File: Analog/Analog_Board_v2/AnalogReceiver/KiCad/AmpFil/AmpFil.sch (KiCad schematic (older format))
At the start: 47 parts, among them P1 CONN_01X02, P10 CONN_01X02, P11 CONN_01X02, P2 CONN_01X02, P3 CONN_01X02, P4 CONN_01X02, P5 CONN_01X02, P6 CONN_01X02, P7 CONN_01X02, P8 CONN_01X02, P9 CONN_01X02, U1 LT1677, U2 SiPM, U3 LT1677, U4 LT1677, U5 LT1677

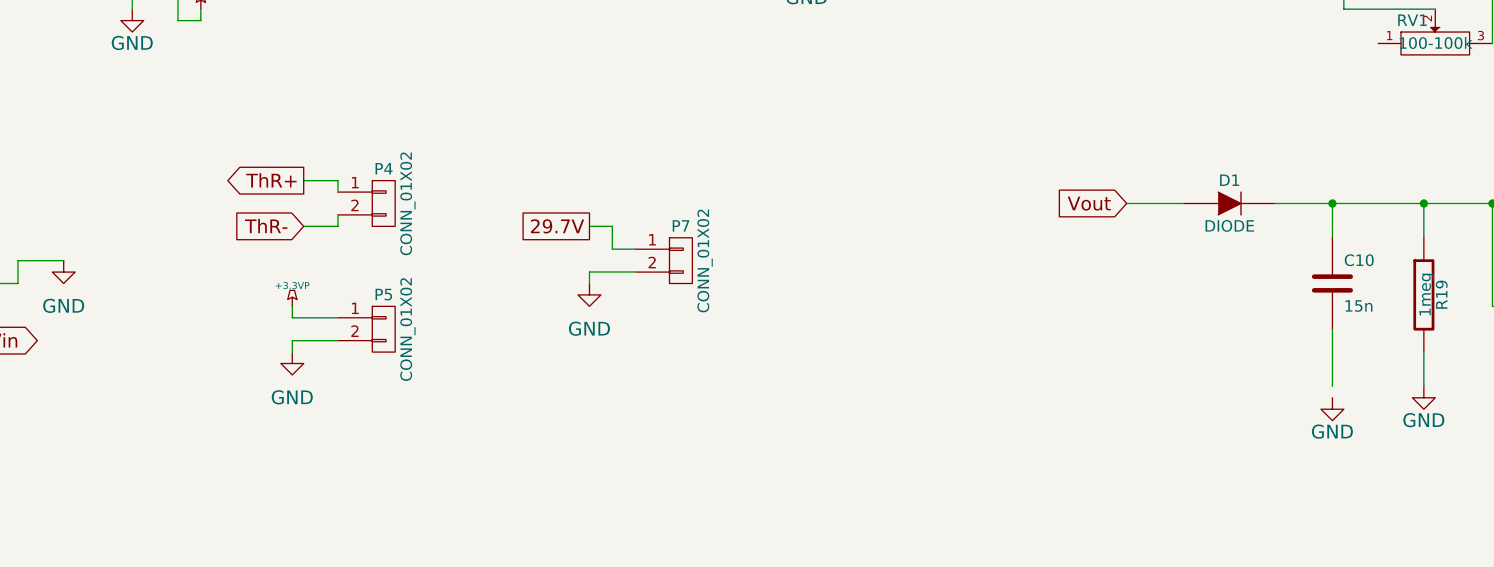
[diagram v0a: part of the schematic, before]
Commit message: New Cutoffs
I tweaked the designs to give different cutoff frequencies and ripple
levels.
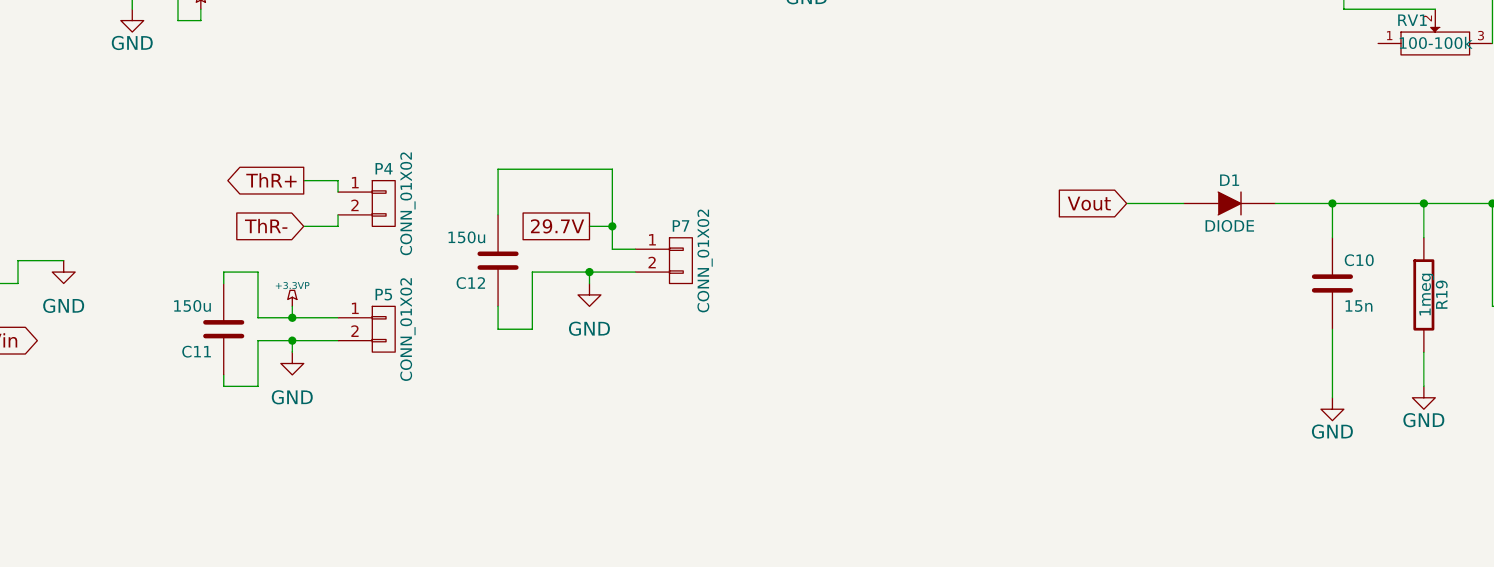
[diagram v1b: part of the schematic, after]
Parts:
- added C11, C12: 150u, symbol C
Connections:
- net +3.3VP: now also C11.2
- net 29.7V: now also C12.2
- net GND: now also C10.2, C11.1, C12.1
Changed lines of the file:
@@
 $EndComp
 $Comp
-L GND #PWR2
+L GND #PWR01
 U 1 1 54DB8B2B
 P 1300 2450
-F 0 "#PWR2" H 1300 2200 60  0001 C CNN
+F 0 "#PWR01" H 1300 2200 60  0001 C CNN
 F 1 "GND" H 1300 2300 60  0000 C CNN
 F 2 "" H 1300 2450 60  0000 C CNN
@@
 $EndComp
 $Comp
-L GND #PWR3
+L GND #PWR02
 U 1 1 54DB8B4B
 P 1600 1450
-F 0 "#PWR3" H 1600 1200 60  0001 C CNN
+F 0 "#PWR02" H 1600 1200 60  0001 C CNN
 F 1 "GND" H 1600 1250 60  0000 C CNN
 F 2 "" H 1600 1450 60  0000 C CNN
@@
 $EndComp
 $Comp
-L GND #PWR5
+L GND #PWR03
 U 1 1 54DB8B6B
 P 2250 1750
-F 0 "#PWR5" H 2250 1500 60  0001 C CNN
+F 0 "#PWR03" H 2250 1500 60  0001 C CNN
 F 1 "GND" H 2250 1600 60  0000 C CNN
 F 2 "" H 2250 1750 60  0000 C CNN
@@
 $EndComp
 $Comp
-L +3.3VP #PWR4
+L +3.3VP #PWR04
 U 1 1 54DB8B8B
 P 1850 1450
-F 0 "#PWR4" H 1900 1480 20  0001 C CNN
+F 0 "#PWR04" H 1900 1480 20  0001 C CNN
 F 1 "+3.3VP" H 1850 1540 30  0000 C CNN
 F 2 "" H 1850 1450 60  0000 C CNN
@@
 $EndComp
 $Comp
-L +3.3VP #PWR6
+L +3.3VP #PWR05
 U 1 1 54DB8BBE
 P 2250 2350
-F 0 "#PWR6" H 2300 2380 20  0001 C CNN
+F 0 "#PWR05" H 2300 2380 20  0001 C CNN
 F 1 "+3.3VP" H 2250 2440 30  0000 C CNN
 F 2 "" H 2250 2350 60  0000 C CNN
@@
 $EndComp
 $Comp
-L +3.3VP #PWR1
+L +3.3VP #PWR06
 U 1 1 54DB8BDE
 P 1100 2350
-F 0 "#PWR1" H 1150 2380 20  0001 C CNN
+F 0 "#PWR06" H 1150 2380 20  0001 C CNN
 F 1 "+3.3VP" H 1100 2440 30  0000 C CNN
 F 2 "" H 1100 2350 60  0000 C CNN
@@
 $EndComp
 $Comp
-L GND #PWR10
+L GND #PWR07
 U 1 1 54DBE1F2
 P 3950 2750
-F 0 "#PWR10" H 3950 2500 60  0001 C CNN
+F 0 "#PWR07" H 3950 2500 60  0001 C CNN
 F 1 "GND" H 3950 2600 60  0000 C CNN
 F 2 "" H 3950 2750 60  0000 C CNN
@@
 $EndComp
 $Comp
-L GND #PWR12
+L GND #PWR08
 U 1 1 54DBE232
 P 4550 1900
-F 0 "#PWR12" H 4550 1650 60  0001 C CNN
+F 0 "#PWR08" H 4550 1650 60  0001 C CNN
 F 1 "GND" H 4550 1750 60  0000 C CNN
 F 2 "" H 4550 1900 60  0000 C CNN
@@
 $EndComp
 $Comp
-L +3.3VP #PWR11
+L +3.3VP #PWR09
 U 1 1 54DBE272
 P 4250 2750
-F 0 "#PWR11" H 4300 2780 20  0001 C CNN
+F 0 "#PWR09" H 4300 2780 20  0001 C CNN
 F 1 "+3.3VP" H 4250 2840 30  0000 C CNN
 F 2 "" H 4250 2750 60  0000 C CNN
@@
 $EndComp
 $Comp
-L +3.3VP #PWR15
+L +3.3VP #PWR010
 U 1 1 54DBE2B2
 P 4700 2350
-F 0 "#PWR15" H 4750 2380 20  0001 C CNN
+F 0 "#PWR010" H 4750 2380 20  0001 C CNN
 F 1 "+3.3VP" H 4700 2440 30  0000 C CNN
 F 2 "" H 4700 2350 60  0000 C CNN
@@
 Connection ~ 7700 2100
 $Comp
-L GND #PWR16
+L GND #PWR011
 U 1 1 54DC07DF
 P 5950 2500
-F 0 "#PWR16" H 5950 2250 60  0001 C CNN
+F 0 "#PWR011" H 5950 2250 60  0001 C CNN
 F 1 "GND" H 5950 2350 60  0000 C CNN
 F 2 "" H 5950 2500 60  0000 C CNN
@@
 $EndComp
 $Comp
-L GND #PWR18
+L GND #PWR012
 U 1 1 54DC0824
 P 6900 2550
-F 0 "#PWR18" H 6900 2300 60  0001 C CNN
+F 0 "#PWR012" H 6900 2300 60  0001 C CNN
 F 1 "GND" H 6900 2400 60  0000 C CNN
 F 2 "" H 6900 2550 60  0000 C CNN
@@
 $EndComp
 $Comp
-L GND #PWR19
+L GND #PWR013
 U 1 1 54DC098B
 P 7350 1850
-F 0 "#PWR19" H 7350 1600 60  0001 C CNN
+F 0 "#PWR013" H 7350 1600 60  0001 C CNN
 F 1 "GND" H 7350 1700 60  0000 C CNN
 F 2 "" H 7350 1850 60  0000 C CNN
@@
 $EndComp
 $Comp
-L +3.3VP #PWR20
+L +3.3VP #PWR014
 U 1 1 54DC09D0
 P 7500 2350
-F 0 "#PWR20" H 7550 2380 20  0001 C CNN
+F 0 "#PWR014" H 7550 2380 20  0001 C CNN
 F 1 "+3.3VP" H 7500 2440 30  0000 C CNN
 F 2 "" H 7500 2350 60  0000 C CNN
@@
 F2
 $Comp
-L GND #PWR30
+L GND #PWR015
 U 1 1 54DC33CA
 P 10300 2400
-F 0 "#PWR30" H 10300 2150 60  0001 C CNN
+F 0 "#PWR015" H 10300 2150 60  0001 C CNN
 F 1 "GND" H 10300 2250 60  0000 C CNN
 F 2 "" H 10300 2400 60  0000 C CNN
@@
 $EndComp
 $Comp
-L +3.3VP #PWR13
+L +3.3VP #PWR016
 U 1 1 54DC6EB6
 P 4650 4050
-F 0 "#PWR13" H 4700 4080 20  0001 C CNN
+F 0 "#PWR016" H 4700 4080 20  0001 C CNN
 F 1 "+3.3VP" H 4650 4140 30  0000 C CNN
 F 2 "" H 4650 4050 60  0000 C CNN
@@
 $EndComp
 $Comp
-L GND #PWR14
+L GND #PWR017
 U 1 1 54DC70AC
 P 4650 4250
-F 0 "#PWR14" H 4650 4000 60  0001 C CNN
+F 0 "#PWR017" H 4650 4000 60  0001 C CNN
 F 1 "GND" H 4650 4050 60  0000 C CNN
 F 2 "" H 4650 4250 60  0000 C CNN
@@
 	1850 4350 1750 4350
 $Comp
-L GND #PWR7
+L GND #PWR018
 U 1 1 54DC7B9D
 P 3200 4900
-F 0 "#PWR7" H 3200 4650 60  0001 C CNN
+F 0 "#PWR018" H 3200 4650 60  0001 C CNN
 F 1 "GND" H 3200 4750 60  0000 C CNN
 F 2 "" H 3200 4900 60  0000 C CNN
@@
 Vin
 $Comp
-L GND #PWR9
+L GND #PWR019
 U 1 1 54E525E1
 P 3650 3850
-F 0 "#PWR9" H 3650 3600 60  0001 C CNN
+F 0 "#PWR019" H 3650 3600 60  0001 C CNN
 F 1 "GND" H 3650 3650 60  0000 C CNN
 F 2 "" H 3650 3850 60  0000 C CNN
@@
 Connection ~ 9200 3600
 $Comp
-L GND #PWR24
+L GND #PWR020
 U 1 1 54E5AECF
 P 9200 4450
-F 0 "#PWR24" H 9200 4200 60  0001 C CNN
+F 0 "#PWR020" H 9200 4200 60  0001 C CNN
 F 1 "GND" H 9200 4300 60  0000 C CNN
 F 2 "" H 9200 4450 60  0000 C CNN
@@
 $EndComp
 $Comp
-L GND #PWR26
+L GND #PWR021
 U 1 1 54E5AF2E
 P 9600 4400
-F 0 "#PWR26" H 9600 4150 60  0001 C CNN
+F 0 "#PWR021" H 9600 4150 60  0001 C CNN
 F 1 "GND" H 9600 4250 60  0000 C CNN
 F 2 "" H 9600 4400 60  0000 C CNN
@@
 $EndComp
 Wire Wire Line
-	9200 4150 9200 4400
+	9200 4150 9200 4450
 Wire Wire Line
 	9600 4250 9600 4400
@@
 $EndComp
 $Comp
-L GND #PWR22
+L GND #PWR022
 U 1 1 54E62B9E
 P 8700 2500
-F 0 "#PWR22" H 8700 2250 60  0001 C CNN
+F 0 "#PWR022" H 8700 2250 60  0001 C CNN
 F 1 "GND" H 8700 2350 60  0000 C CNN
 F 2 "" H 8700 2500 60  0000 C CNN
@@
 $EndComp
 $Comp
-L GND #PWR23
+L GND #PWR023
 U 1 1 54E62BA4
 P 9000 1500
-F 0 "#PWR23" H 9000 1250 60  0001 C CNN
+F 0 "#PWR023" H 9000 1250 60  0001 C CNN
 F 1 "GND" H 9000 1300 60  0000 C CNN
 F 2 "" H 9000 1500 60  0000 C CNN
@@
 $EndComp
 $Comp
-L GND #PWR27
+L GND #PWR024
 U 1 1 54E62BAA
 P 9650 1800
-F 0 "#PWR27" H 9650 1550 60  0001 C CNN
+F 0 "#PWR024" H 9650 1550 60  0001 C CNN
 F 1 "GND" H 9650 1650 60  0000 C CNN
 F 2 "" H 9650 1800 60  0000 C CNN
@@
 $EndComp
 $Comp
-L +3.3VP #PWR25
+L +3.3VP #PWR025
 U 1 1 54E62BB0
 P 9250 1500
-F 0 "#PWR25" H 9300 1530 20  0001 C CNN
+F 0 "#PWR025" H 9300 1530 20  0001 C CNN
 F 1 "+3.3VP" H 9250 1590 30  0000 C CNN
 F 2 "" H 9250 1500 60  0000 C CNN
@@
 $EndComp
 $Comp
-L +3.3VP #PWR28
+L +3.3VP #PWR026
 U 1 1 54E62BB6
 P 9650 2400
-F 0 "#PWR28" H 9700 2430 20  0001 C CNN
+F 0 "#PWR026" H 9700 2430 20  0001 C CNN
 F 1 "+3.3VP" H 9650 2490 30  0000 C CNN
 F 2 "" H 9650 2400 60  0000 C CNN
@@
 $EndComp
 $Comp
-L +3.3VP #PWR21
+L +3.3VP #PWR027
 U 1 1 54E62BBC
 P 8500 2400
-F 0 "#PWR21" H 8550 2430 20  0001 C CNN
+F 0 "#PWR027" H 8550 2430 20  0001 C CNN
 F 1 "+3.3VP" H 8500 2490 30  0000 C CNN
 F 2 "" H 8500 2400 60  0000 C CNN
@@
 	4250 2800 4250 2750
 $Comp
-L GND #PWR8
+L GND #PWR028
 U 1 1 54E66CD5
 P 3250 2600
-F 0 "#PWR8" H 3250 2350 60  0001 C CNN
+F 0 "#PWR028" H 3250 2350 60  0001 C CNN
 F 1 "GND" H 3250 2450 60  0000 C CNN
 F 2 "" H 3250 2600 60  0000 C CNN
@@
 $EndComp
 $Comp
-L GND #PWR29
+L GND #PWR029
 U 1 1 54E7CEE2
 P 10000 4350
-F 0 "#PWR29" H 10000 4100 60  0001 C CNN
+F 0 "#PWR029" H 10000 4100 60  0001 C CNN
 F 1 "GND" H 10000 4200 60  0000 C CNN
 F 2 "" H 10000 4350 60  0000 C CNN
@@
 $EndComp
 $Comp
-L GND #PWR17
+L GND #PWR030
 U 1 1 5508AD46
 P 5950 3950
-F 0 "#PWR17" H 5950 3700 60  0001 C CNN
+F 0 "#PWR030" H 5950 3700 60  0001 C CNN
 F 1 "GND" H 5950 3750 60  0000 C CNN
 F 2 "" H 5950 3950 60  0000 C CNN
@@
 $EndComp
 Wire Wire Line
-	6150 3800 6050 3800
-Wire Wire Line
-	6050 3800 6050 3700
+	6050 3800 6150 3800
+Wire Wire Line
+	6050 3450 6050 3800
 Wire Wire Line
 	6050 3700 5950 3700
 Wire Wire Line
-	6150 3900 5950 3900
+	5700 3900 6150 3900
 Wire Wire Line
 	5950 3900 5950 3950
 Wire Wire Line
-	4850 4100 4650 4100
+	4500 4100 4850 4100
 Wire Wire Line
 	4650 4100 4650 4050
 Wire Wire Line
-	4850 4200 4650 4200
+	4500 4200 4850 4200
 Wire Wire Line
 	4650 4200 4650 4250
@@
 Wire Wire Line
 	9900 2600 9900 2900
+$Comp
+L C C12
+U 1 1 5509F4B1
+P 5550 3850
+F 0 "C12" H 5600 3950 50  0000 L CNN
+F 1 "150u" H 5600 3750 50  0000 L CNN
+F 2 "" H 5588 3700 30  0001 C CNN
+F 3 "" H 5550 3850 60  0000 C CNN
+	1    5550 3850
+	-1   0    0    1
+$EndComp
+$Comp
+L C C11
+U 1 1 5509F809
+P 4350 4150
+F 0 "C11" H 4400 4250 50  0000 L CNN
+F 1 "150u" H 4400 4050 50  0000 L CNN
+F 2 "" H 4388 4000 30  0001 C CNN
+F 3 "" H 4350 4150 60  0000 C CNN
+	1    4350 4150
+	-1   0    0    1
+$EndComp
+Wire Wire Line
+	6050 3450 5550 3450
+Wire Wire Line
+	5550 3450 5550 3650
+Connection ~ 6050 3700
+Wire Wire Line
+	5700 3900 5700 4150
+Wire Wire Line
+	5700 4150 5550 4150
+Wire Wire Line
+	5550 4150 5550 4050
+Connection ~ 5950 3900
+Wire Wire Line
+	4500 4100 4500 3900
+Wire Wire Line
+	4500 3900 4350 3900
+Wire Wire Line
+	4350 3900 4350 3950
+Connection ~ 4650 4100
+Wire Wire Line
+	4500 4200 4500 4400
+Wire Wire Line
+	4500 4400 4350 4400
+Wire Wire Line
+	4350 4400 4350 4350
+Connection ~ 4650 4200
 $EndSCHEMATC
